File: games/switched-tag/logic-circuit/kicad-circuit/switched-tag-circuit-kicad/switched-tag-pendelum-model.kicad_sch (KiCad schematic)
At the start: 7 parts

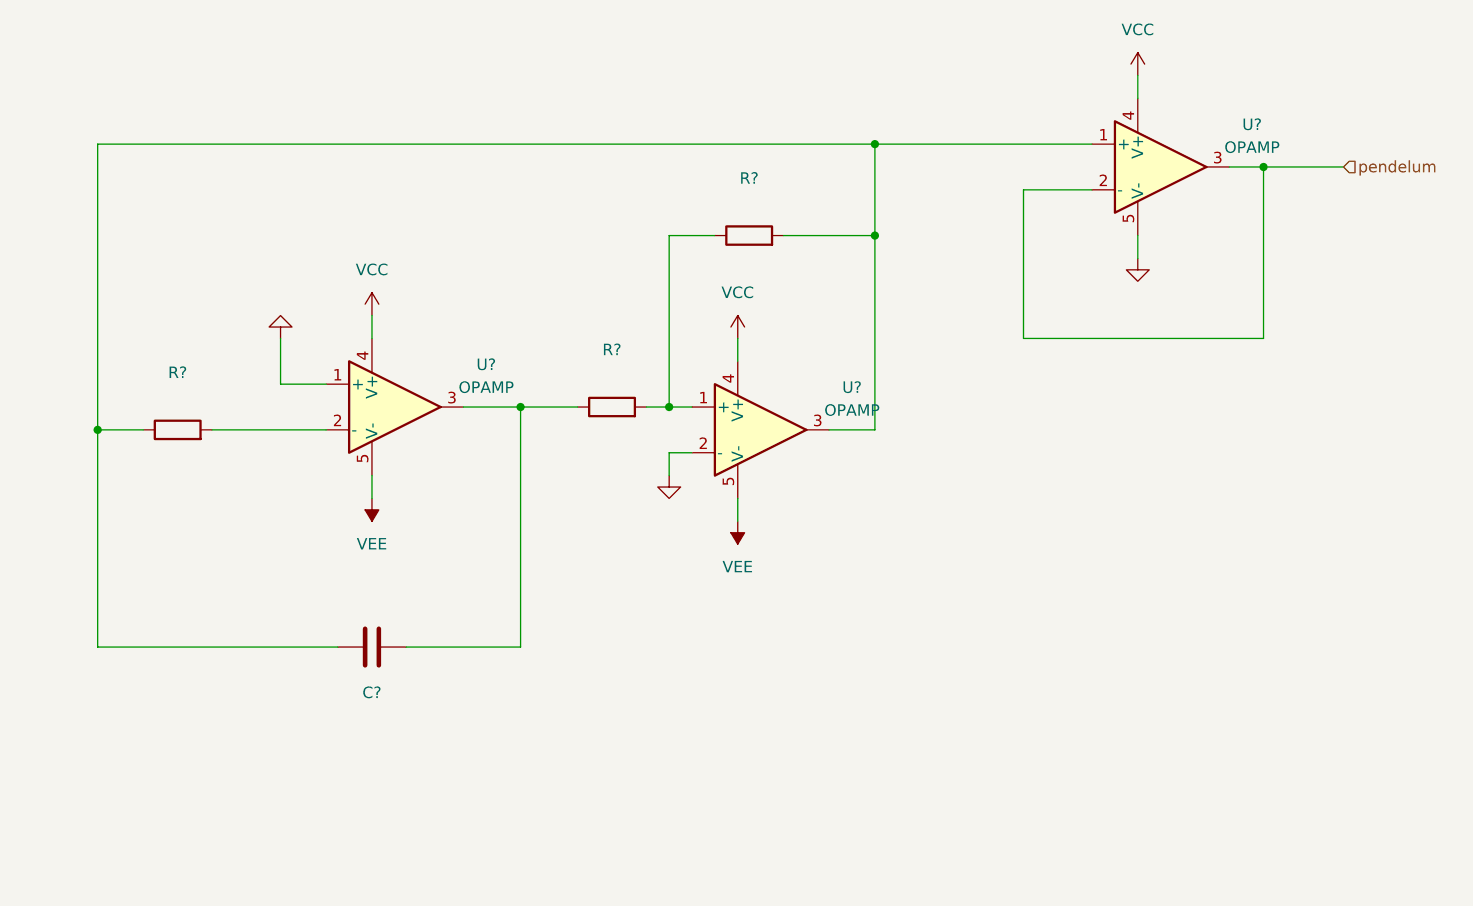
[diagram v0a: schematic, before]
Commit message: Saving progress on kicad schematic. Trying to set up ngspice simulation.
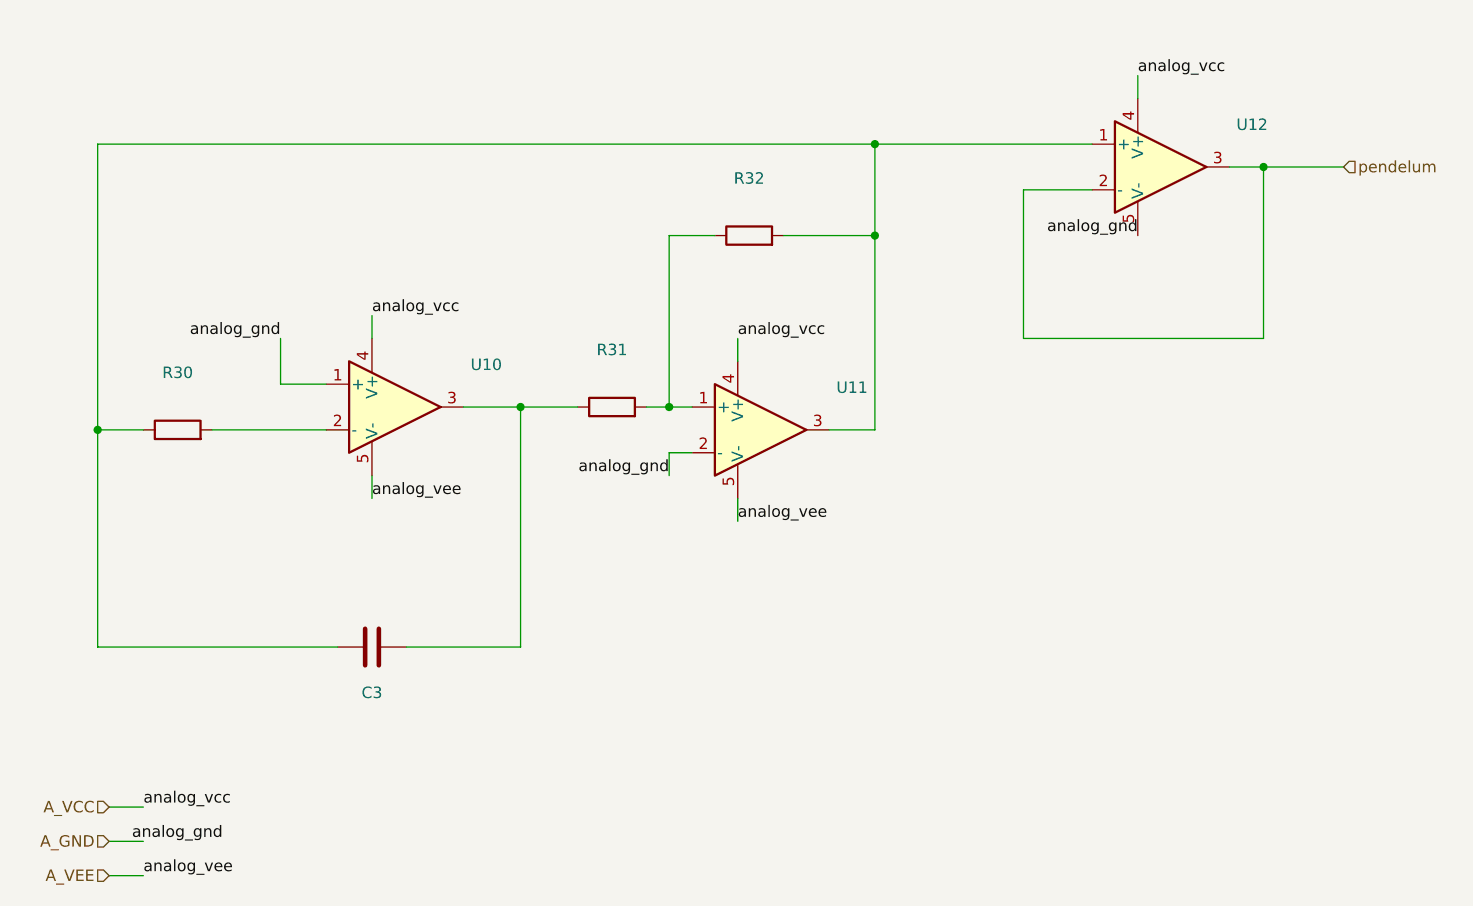
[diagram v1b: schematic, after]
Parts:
- U10, U11, U12: renamed from U?; value OPAMP -> (none); Spice_Lib_File (none) -> /home/pab/Inventions/analog-circuit-game-console/ms-circuit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; Spice_Model (none) -> LM358; Spice_Node_Sequence (none) -> 1 2 4 5 3
- gave numbers to parts that had none: 4
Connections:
- net GND renamed A_GND
- net VCC renamed A_VCC
- net VEE renamed A_VEE

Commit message: Fixed problems with kicad circuit adn spice setup.
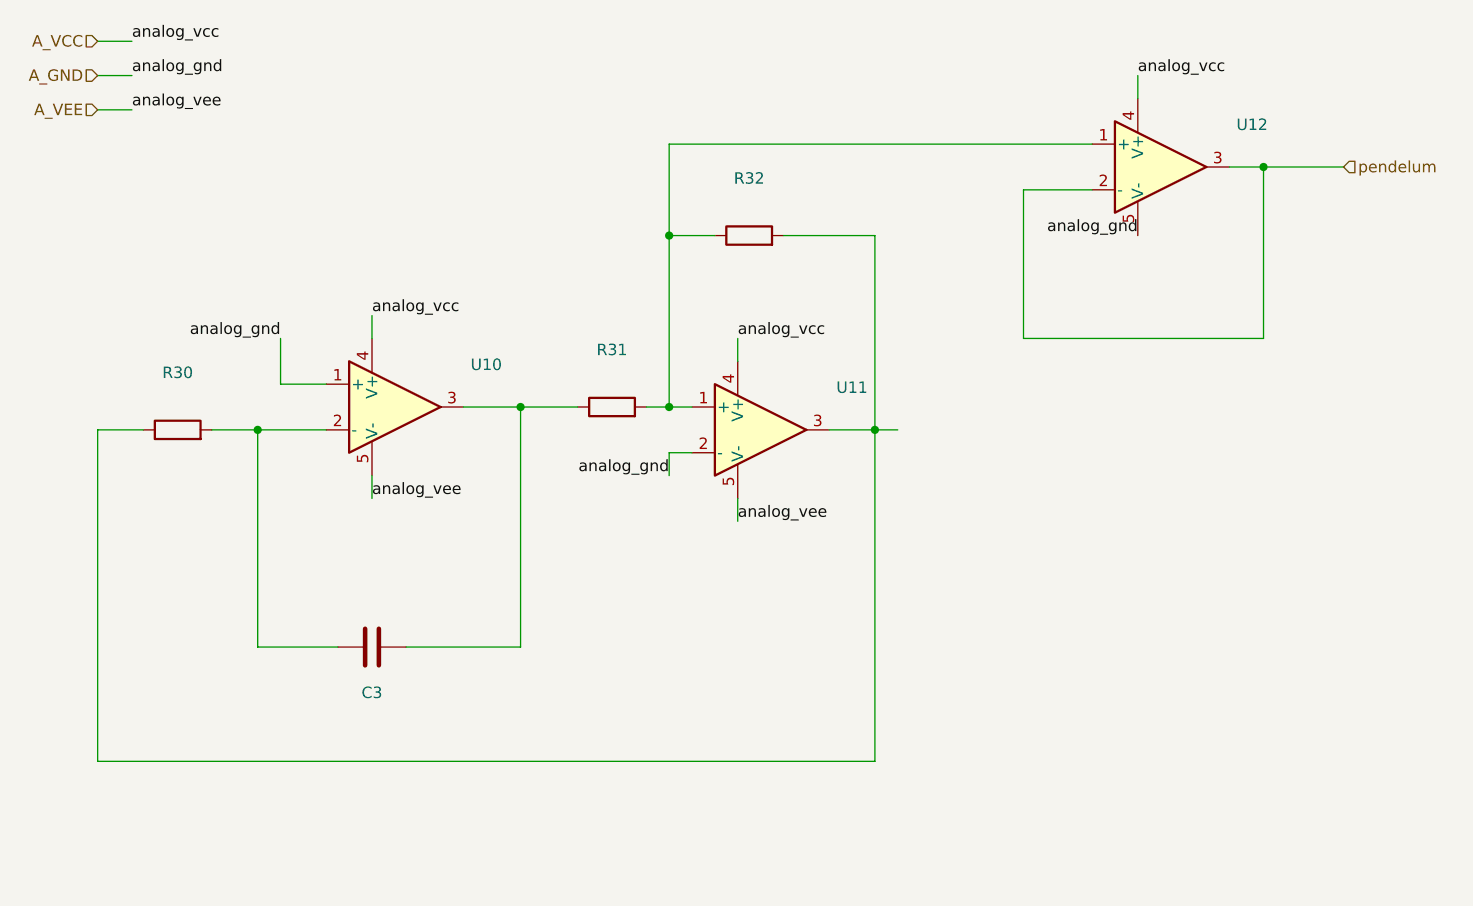
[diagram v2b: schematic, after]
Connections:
- net at R30.1, R32.2, U11.3: no longer C3.1, U12.1 (+)
- net at R30.2, U10.2 (-): now also C3.1
- net at R31.2, R32.1, U11.1 (+): now also U12.1 (+)
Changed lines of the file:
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@@
   (junction (at 109.22 85.09) (diameter 0) (color 0 0 0 0)
   )
-  (junction (at 45.72 87.63) (diameter 0) (color 0 0 0 0)
-  )
-  (junction (at 132.08 55.88) (diameter 0) (color 0 0 0 0)
-  )
-  (junction (at 132.08 66.04) (diameter 0) (color 0 0 0 0)
+  (junction (at 132.08 87.63) (diameter 0) (color 0 0 0 0)
   )
   (junction (at 92.71 85.09) (diameter 0) (color 0 0 0 0)
   )
-  (wire (pts (xy 45.72 55.88) (xy 45.72 87.63))
-    (stroke (width 0) (type default) (color 0 0 0 0))
+  (junction (at 63.5 87.63) (diameter 0) (color 0 0 0 0)
   )
-  (wire (pts (xy 46.99 133.35) (xy 50.8 133.35))
-    (stroke (width 0) (type default) (color 0 0 0 0))
+  (junction (at 109.22 66.04) (diameter 0) (color 0 0 0 0)
   )
-  (wire (pts (xy 132.08 55.88) (xy 156.21 55.88))
+  (wire (pts (xy 45.72 48.26) (xy 49.53 48.26))
     (stroke (width 0) (type default) (color 0 0 0 0))
   )
@@
     (stroke (width 0) (type default) (color 0 0 0 0))
   )
+  (wire (pts (xy 63.5 111.76) (xy 63.5 87.63))
+    (stroke (width 0) (type default) (color 0 0 0 0))
+  )
   (wire (pts (xy 71.12 82.55) (xy 66.04 82.55))
     (stroke (width 0) (type default) (color 0 0 0 0))
@@
     (stroke (width 0) (type default) (color 0 0 0 0))
   )
-  (wire (pts (xy 45.72 87.63) (xy 45.72 111.76))
-    (stroke (width 0) (type default) (color 0 0 0 0))
-  )
-  (wire (pts (xy 58.42 87.63) (xy 71.12 87.63))
+  (wire (pts (xy 58.42 87.63) (xy 63.5 87.63))
     (stroke (width 0) (type default) (color 0 0 0 0))
   )
   (wire (pts (xy 161.29 48.26) (xy 161.29 50.8))
-    (stroke (width 0) (type default) (color 0 0 0 0))
-  )
-  (wire (pts (xy 132.08 66.04) (xy 132.08 55.88))
     (stroke (width 0) (type default) (color 0 0 0 0))
   )
@@
     (stroke (width 0) (type default) (color 0 0 0 0))
   )
+  (wire (pts (xy 132.08 87.63) (xy 134.62 87.63))
+    (stroke (width 0) (type default) (color 0 0 0 0))
+  )
+  (wire (pts (xy 72.39 111.76) (xy 63.5 111.76))
+    (stroke (width 0) (type default) (color 0 0 0 0))
+  )
+  (wire (pts (xy 109.22 55.88) (xy 156.21 55.88))
+    (stroke (width 0) (type default) (color 0 0 0 0))
+  )
   (wire (pts (xy 114.3 66.04) (xy 109.22 66.04))
     (stroke (width 0) (type default) (color 0 0 0 0))
   )
-  (wire (pts (xy 46.99 137.16) (xy 50.8 137.16))
+  (wire (pts (xy 45.72 52.07) (xy 49.53 52.07))
     (stroke (width 0) (type default) (color 0 0 0 0))
   )
@@
     (stroke (width 0) (type default) (color 0 0 0 0))
   )
+  (wire (pts (xy 132.08 124.46) (xy 45.72 124.46))
+    (stroke (width 0) (type default) (color 0 0 0 0))
+  )
+  (wire (pts (xy 45.72 124.46) (xy 45.72 87.63))
+    (stroke (width 0) (type default) (color 0 0 0 0))
+  )
   (wire (pts (xy 156.21 60.96) (xy 148.59 60.96))
     (stroke (width 0) (type default) (color 0 0 0 0))
@@
     (stroke (width 0) (type default) (color 0 0 0 0))
   )
+  (wire (pts (xy 109.22 55.88) (xy 109.22 66.04))
+    (stroke (width 0) (type default) (color 0 0 0 0))
+  )
   (wire (pts (xy 132.08 87.63) (xy 132.08 66.04))
     (stroke (width 0) (type default) (color 0 0 0 0))
   )
-  (wire (pts (xy 45.72 111.76) (xy 72.39 111.76))
+  (wire (pts (xy 132.08 87.63) (xy 132.08 124.46))
     (stroke (width 0) (type default) (color 0 0 0 0))
   )
@@
     (stroke (width 0) (type default) (color 0 0 0 0))
   )
-  (wire (pts (xy 106.68 85.09) (xy 109.22 85.09))
+  (wire (pts (xy 63.5 87.63) (xy 71.12 87.63))
     (stroke (width 0) (type default) (color 0 0 0 0))
   )
-  (wire (pts (xy 132.08 55.88) (xy 45.72 55.88))
+  (wire (pts (xy 106.68 85.09) (xy 109.22 85.09))
     (stroke (width 0) (type default) (color 0 0 0 0))
   )
@@
     (stroke (width 0) (type default) (color 0 0 0 0))
   )
-  (wire (pts (xy 46.99 129.54) (xy 50.8 129.54))
+  (wire (pts (xy 45.72 44.45) (xy 49.53 44.45))
     (stroke (width 0) (type default) (color 0 0 0 0))
   )
@@
     (effects (font (size 1.27 1.27)) (justify left bottom))
   )
-  (label "analog_vcc" (at 50.8 129.54 0)
+  (label "analog_vcc" (at 49.53 44.45 0)
     (effects (font (size 1.27 1.27)) (justify left bottom))
   )
@@
     (effects (font (size 1.27 1.27)) (justify left bottom))
   )
-  (label "analog_gnd" (at 49.53 133.35 0)
+  (label "analog_gnd" (at 49.53 48.26 0)
     (effects (font (size 1.27 1.27)) (justify left bottom))
   )
@@
     (effects (font (size 1.27 1.27)) (justify right bottom))
   )
-  (label "analog_vee" (at 50.8 137.16 0)
+  (label "analog_vee" (at 49.53 52.07 0)
     (effects (font (size 1.27 1.27)) (justify left bottom))
   )
-  (hierarchical_label "A_GND" (shape input) (at 46.99 133.35 180)
+  (hierarchical_label "A_GND" (shape input) (at 45.72 48.26 180)
     (effects (font (size 1.27 1.27)) (justify right))
   )
@@
     (effects (font (size 1.27 1.27)) (justify left))
   )
-  (hierarchical_label "A_VCC" (shape input) (at 46.99 129.54 180)
+  (hierarchical_label "A_VCC" (shape input) (at 45.72 44.45 180)
     (effects (font (size 1.27 1.27)) (justify right))
   )
-  (hierarchical_label "A_VEE" (shape input) (at 46.99 137.16 180)
+  (hierarchical_label "A_VEE" (shape input) (at 45.72 52.07 180)
     (effects (font (size 1.27 1.27)) (justify right))
   )
